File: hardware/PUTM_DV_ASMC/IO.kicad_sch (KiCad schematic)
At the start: 0 parts

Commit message: io section
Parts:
- added C29, C30: 100n, Capacitor_SMD:C_0603_1608Metric_Pad1.08x0.95mm_HandSolder, symbol Device:C_Small
- added Q?: BUK6D210, Local_Library:Diodes_UDFN2020-6_Type-F, symbol BUK6D210:BUK6D210
- added R3, R5: 2k, Resistor_SMD:R_0603_1608Metric_Pad0.98x0.95mm_HandSolder, symbol Device:R_Small
- added R4, R8: 10k, Resistor_SMD:R_0603_1608Metric_Pad0.98x0.95mm_HandSolder, symbol Device:R_Small
- added R?: 100R, Resistor_SMD:R_0603_1608Metric, symbol Device:R_Small
- added R?: 10k, Resistor_SMD:R_0603_1608Metric, symbol Device:R_Small
- added TP?: TestPoint_Small, TestPoint:TestPoint_Pad_D1.0mm, symbol Connector:TestPoint_Small
- added U3, U4: TLP291-4, Package_SO:SOIC-16_4.55x10.3mm_P1.27mm, symbol Isolator:TLP291-4
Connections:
- new net: Q?.3 (G), R?.1, R?.2, TP?.1
- new net: C30.1, R5.2, U4.1
- new net: C29.1, R3.2, U3.1
- new net +3.3V: R4.1, R8.1
- new net AS_SAFETY: R3.1
- new net AS_SENSE: R4.2, U3.16
- new net GND: C29.2, C30.2, Q?.4 (S), Q?.8 (S), R?.1, U3.15, U3.2, U4.15, U4.2
- new net IN_BUZZER: R?.2
- new net OUT_BUZZER: Q?.1 (D), Q?.2 (D), Q?.5 (D), Q?.6 (D), Q?.7 (D)
- new net RES_SAFETY: R5.1
- new net RES_SENSE: R8.2, U4.16
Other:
- note added: "+24V"
- note added: "Buzzer"
- note added: "Buzzer Section"
- note added: "Safety Sensig"
- title: (none) -> Input/Output Section

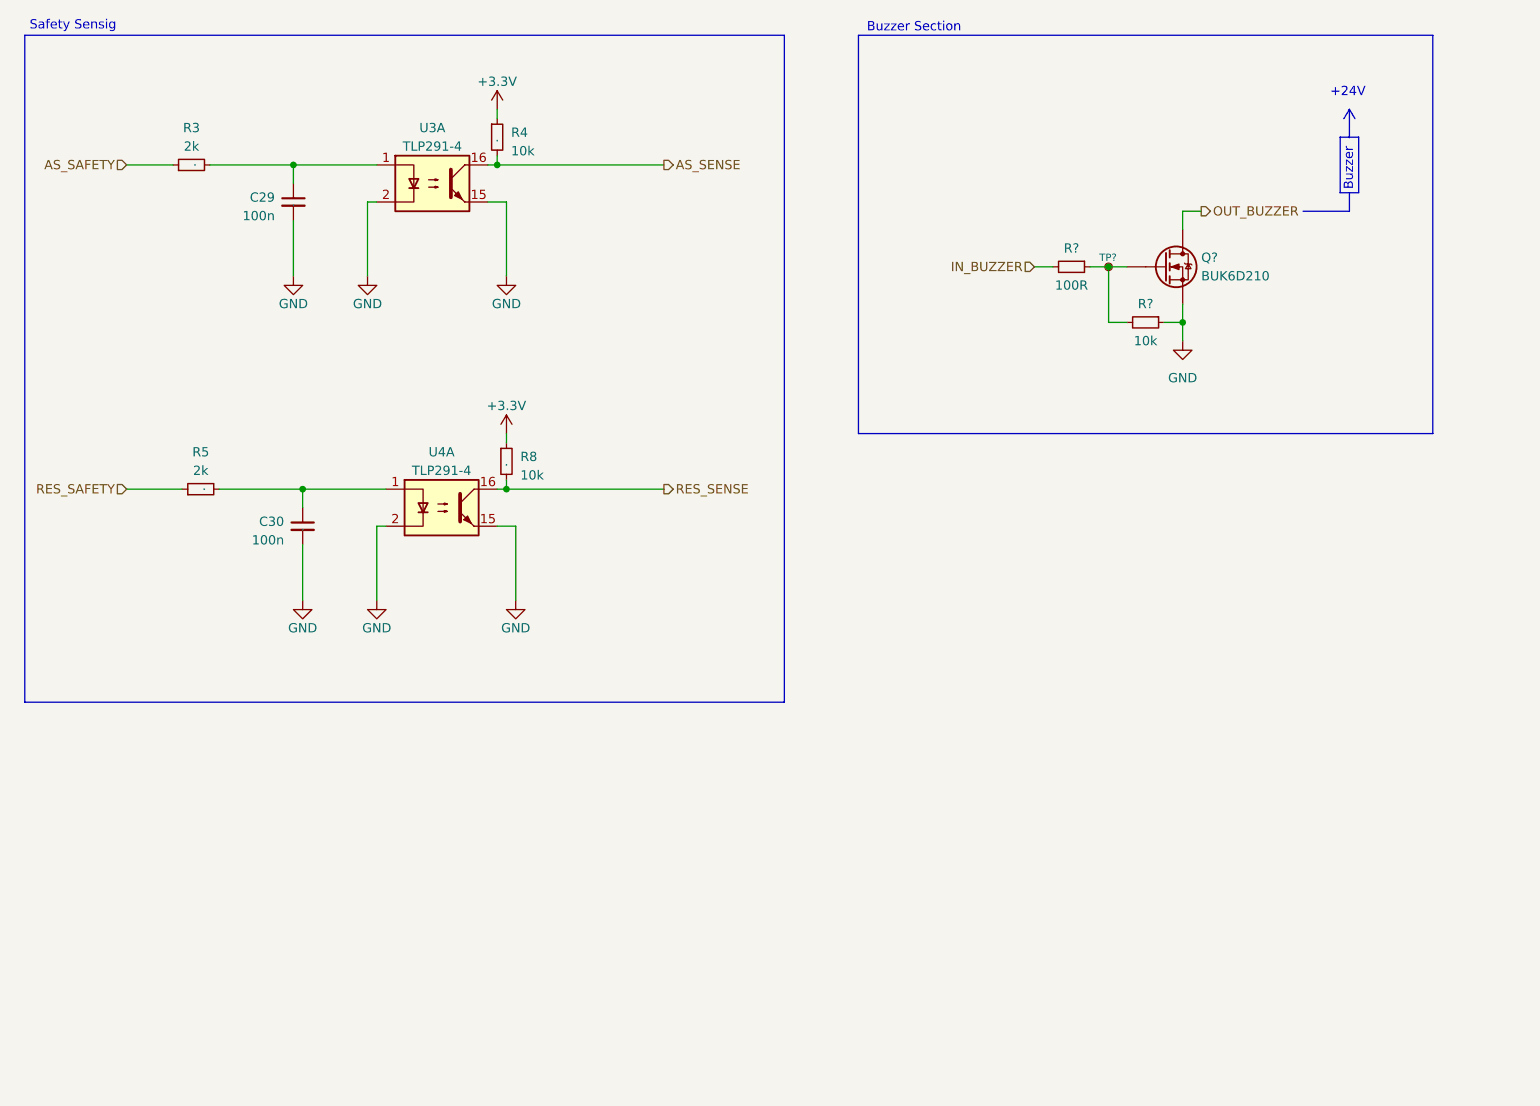
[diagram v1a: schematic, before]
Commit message: schematics without main connector
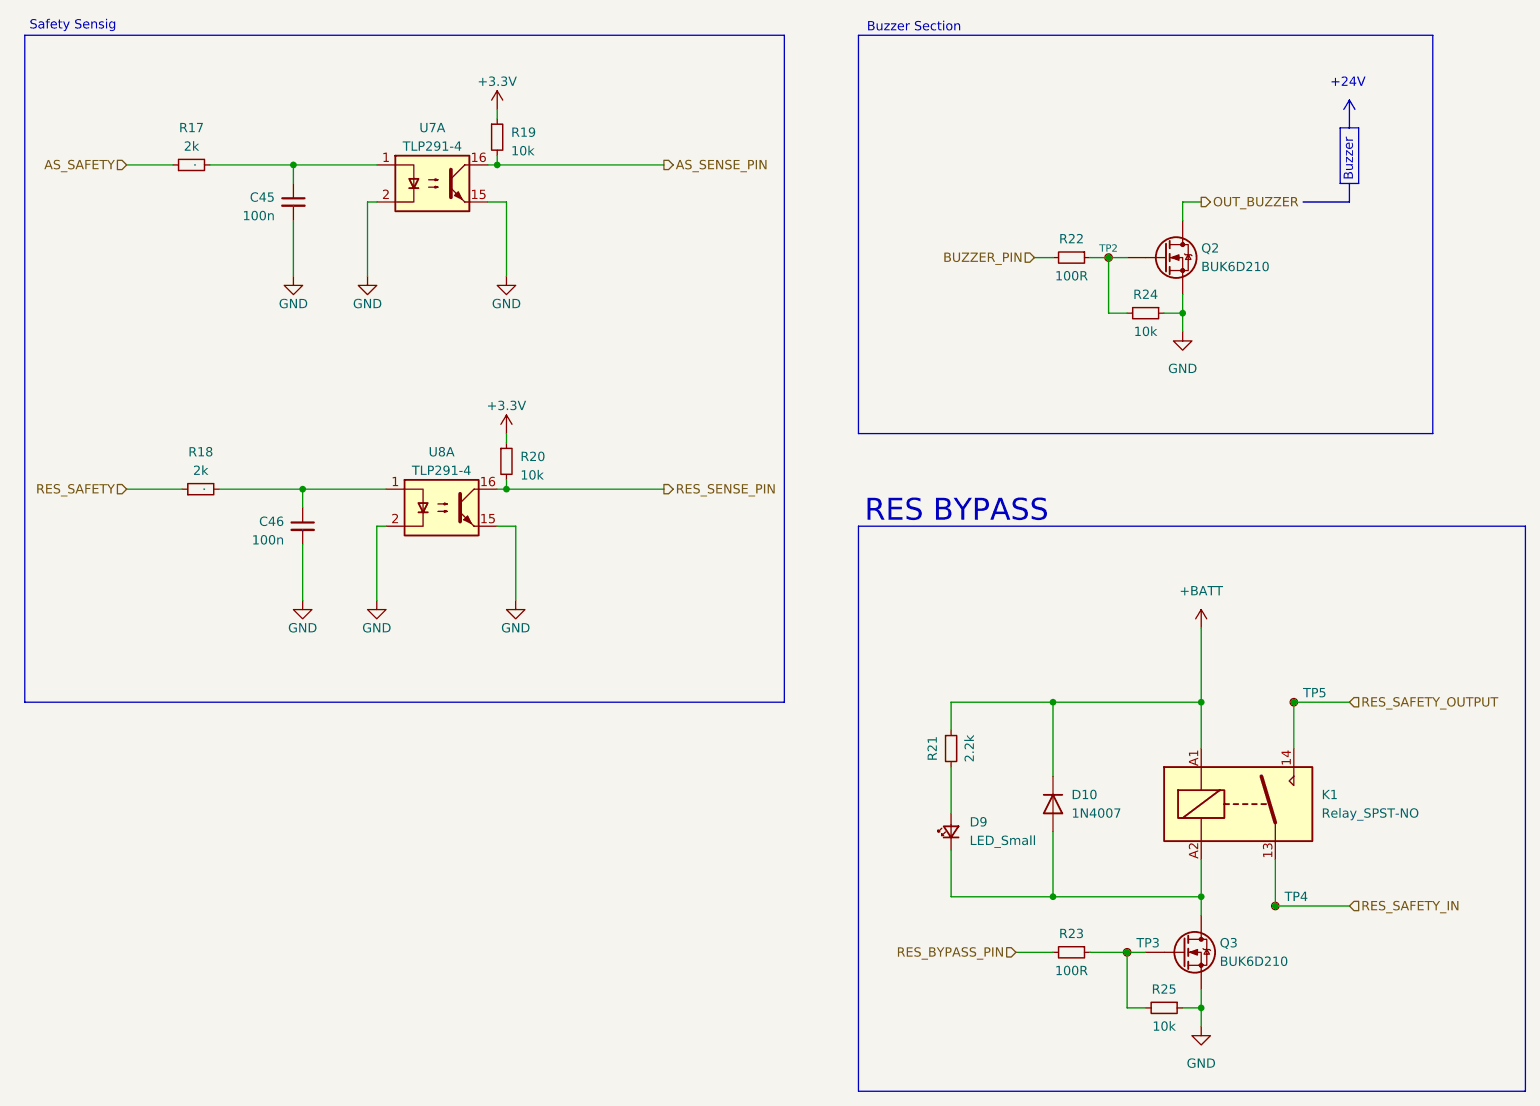
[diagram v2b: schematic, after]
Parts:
- added D10: 1N4007, Diode_THT:D_DO-41_SOD81_P10.16mm_Horizontal, symbol Diode:1N4007
- added D9: LED_Small, symbol Device:LED_Small
- added K1: Relay_SPST-NO, symbol Relay:Relay_SPST-NO
- added Q3: BUK6D210, Local_Library:Diodes_UDFN2020-6_Type-F, symbol BUK6D210:BUK6D210
- added R21: 2.2k, Resistor_SMD:R_1206_3216Metric_Pad1.30x1.75mm_HandSolder, symbol Device:R_Small
- added R23: 100R, Resistor_SMD:R_0603_1608Metric, symbol Device:R_Small
- added R25: 10k, Resistor_SMD:R_0603_1608Metric, symbol Device:R_Small
- added TP3, TP4, TP5: TestPoint_Small, symbol Connector:TestPoint_Small
- gave numbers to parts that had none: 4
- renumbered C29 to C45, C30 to C46, R3 to R17, R5 to R18, R4 to R19, R8 to R20, U3 to U7, U4 to U8
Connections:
- net GND: now also Q3.4 (S), Q3.8 (S), R25.1
- net AS_SENSE renamed AS_SENSE_PIN
- net IN_BUZZER renamed BUZZER_PIN
- net RES_SENSE renamed RES_SENSE_PIN
- new net: Q3.3 (G), R23.1, R25.2, TP3.1
- new net: D10.2 (A), D9.1 (K), K1.A2, Q3.1 (D), Q3.2 (D), Q3.5 (D), Q3.6 (D), Q3.7 (D)
- new net: D9.2 (A), R21.2
- new net +BATT: D10.1 (K), K1.A1, R21.1
- new net RES_BYPASS_PIN: R23.2
- new net RES_SAFETY_IN: K1.13, TP4.1
- new net RES_SAFETY_OUTPUT: K1.14, TP5.1
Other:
- note added: "RES BYPASS"
- moved on the sheet: Q2, R22, R24, TP2

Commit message: done schematic v1
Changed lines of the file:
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@@
 	)
 	(hierarchical_label "RES_SAFETY_OUTPUT"
-		(shape input)
+		(shape output)
 		(at 201.93 109.22 0)
 		(effects
@@
 	)
 	(hierarchical_label "RES_SAFETY_IN"
-		(shape input)
+		(shape output)
 		(at 201.93 137.16 0)
 		(effects
@@
 		)
 	)
-	(group ""
-		(members "058c119b-7b5e-4be6-9dd9-77956af8631e" "06eb6851-f71e-48c3-9d55-6a4454f72066"
-			"0f04764c-a9c6-4546-b0f8-8e79def7ef79" "1be2d804-d21b-42bf-9922-a1e309fc6313"
-			"20d4376f-85fc-438f-80fd-76ed747431a7" "2517ebd4-1633-4649-af89-dcdf95830b6f"
-			"2883a0e1-238c-42ef-9bbf-5d3af29825bc" "334e8cb6-5bb3-435d-9903-589fd98b6398"
-			"3df0cd19-b65c-417f-a0fd-361945718dc4" "3eab420e-4a45-4a70-855a-c900c3a10dd2"
-			"3fe88a36-0125-48db-a28f-10e085086908" "4a3b0eae-4bff-4e5b-a0b4-a98859ab8fae"
-			"4c7c4c9c-1cf3-4004-9802-0db4d4e54b92" "51e78d01-08dc-4f48-afe4-2cb2bb5cd559"
-			"58fcd43b-4f94-4f07-8bf2-a616202ffac8" "5c459c4a-ac80-46d9-b66f-ce0857e02798"
-			"6d31a3b8-99e6-4b49-8c53-aff4336e20b8" "6dbf84d3-72af-48e1-92f4-2f8d24832782"
-			"7048251e-2d57-4c7a-abd6-8eb55bf87aa3" "a109052a-2f62-481d-8364-96d638b9e39b"
-			"a16fcd44-259b-4214-93f9-ce0456dfff68" "a55c4ed3-f659-4865-82be-744633d19361"
-			"ab5d48bf-d740-4920-b823-31d1c89de7ce" "ab722c10-840f-46a0-89b6-ca8210a4b5f0"
-			"b00dd03d-f6f1-4cee-8322-05d2814af237" "bd5c868e-759a-451f-a8fa-e3902719da1d"
-			"d454ba87-598c-4b5e-ae94-e0a08750598a" "e149af7e-e9bc-482f-837a-7105fe1d689c"
-			"e560e48f-4926-43a8-aca3-5d48b251c2f7" "e86e67bc-af59-4abf-91fb-ea473bbc48ce"
-			"f8eda6d1-aa82-4881-a45a-fa8cb19e135d"
-		)
-	)

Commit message: schematic without error
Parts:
- removed U7: TLP291-4, Package_SO:SOIC-16_4.55x10.3mm_P1.27mm, symbol Isolator:TLP291-4
- added unit 2 of U8
- Q2, Q3: footprint Local_Library:Diodes_UDFN2020-6_Type-F -> UDFN2020-6:Diodes_UDFN2020-6_Type-F
- U8: Mouser Part Number 757-TLP293-4TPRE -> (none)
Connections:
- net AS_SENSE_PIN: now also U8.16
- net GND: now also U8.13, U8.4
- net RES_SENSE_PIN: now also U8.14; no longer U8.16
- net at C46.1, R18.2: now also U8.3; no longer U8.1
- net at C45.1, R17.2: now also U8.1

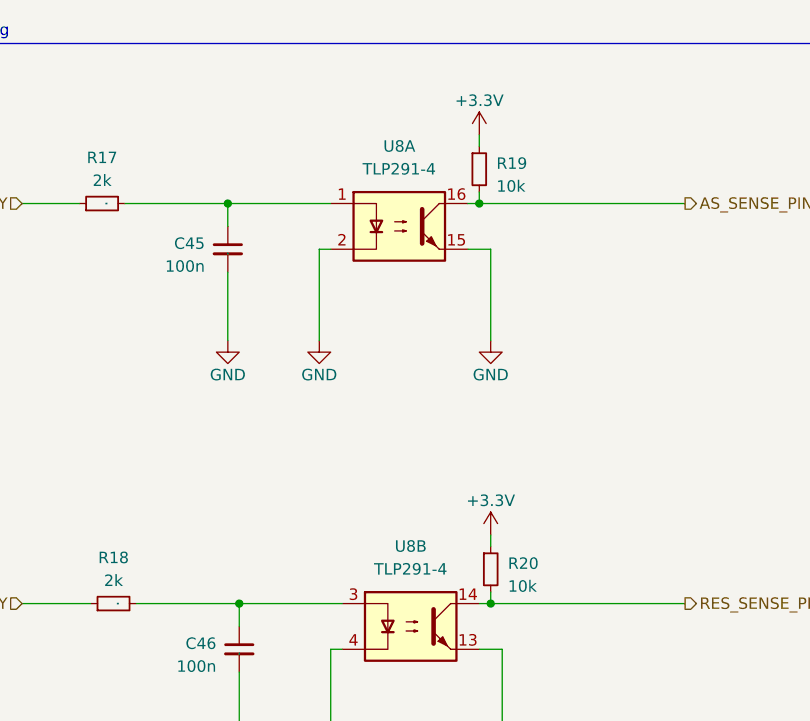
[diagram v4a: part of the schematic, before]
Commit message: tylko dwa bledy z can - schemat na wykonczeniu
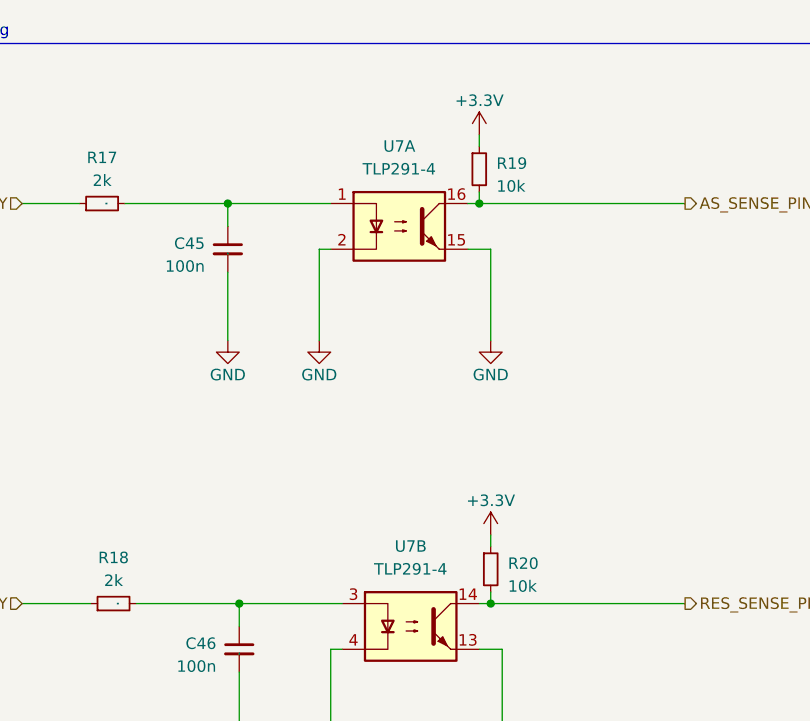
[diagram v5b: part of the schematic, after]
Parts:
- renumbered U8 to U7
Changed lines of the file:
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@@
 		(dnp no)
 		(fields_autoplaced yes)
-		(property "Reference" "U8"
+		(property "Reference" "U7"
 			(at 77.47 73.66 0)
 			(show_name no)
@@
 			(project "PUTM_DV_ASMC"
 				(path "/b652b05a-4e3d-4ad1-b032-18886abe7d45/758e311c-7b96-4a6d-a057-b3755526b6e1"
-					(reference "U8")
+					(reference "U7")
 					(unit 2)
 				)
@@
 		(dnp no)
 		(fields_autoplaced yes)
-		(property "Reference" "U8"
+		(property "Reference" "U7"
 			(at 76.2 29.21 0)
 			(show_name no)
@@
 			(project "PUTM_DV_ASMC"
 				(path "/b652b05a-4e3d-4ad1-b032-18886abe7d45/758e311c-7b96-4a6d-a057-b3755526b6e1"
-					(reference "U8")
-					(unit 1)
-				)
+					(reference "U7")
+					(unit 1)
+				)

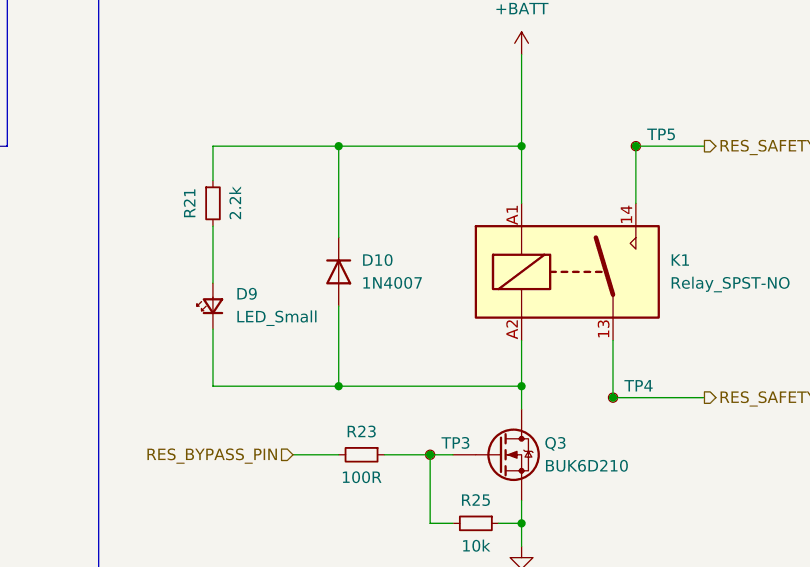
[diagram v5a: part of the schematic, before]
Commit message: poprawki footprint
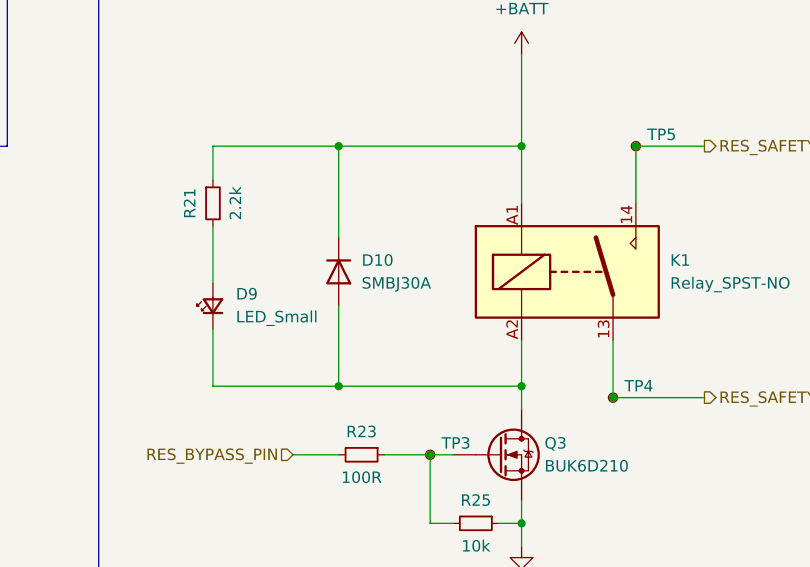
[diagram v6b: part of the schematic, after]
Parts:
- D10: value 1N4007 -> SMBJ30A; footprint Diode_THT:D_DO-41_SOD81_P10.16mm_Horizontal -> Diode_SMD:D_SMB_Handsoldering
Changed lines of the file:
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@@
 			)
 		)
-		(property "Value" "1N4007"
+		(property "Value" "SMBJ30A"
 			(at 163.83 124.4599 90)
 			(show_name no)
@@
 			)
 		)
-		(property "Footprint" "Diode_THT:D_DO-41_SOD81_P10.16mm_Horizontal"
+		(property "Footprint" "Diode_SMD:D_SMB_Handsoldering"
 			(at 156.845 123.19 0)
 			(hide yes)
@@
 			)
 		)
-		(property "Datasheet" "http://www.vishay.com/docs/88503/1n4001.pdf"
+		(property "Datasheet" "https://www.vishay.com/docs/88392/smbj.pdf"
 			(at 161.29 123.19 0)
 			(hide yes)
@@
 			)
 		)
-		(property "Description" "1000V 1A General Purpose Rectifier Diode, DO-41"
+		(property "Description" "ESD Protection Diodes / TVS Diodes 30V 1000W UniDir TransZorb 5% Tol"
 			(at 161.29 123.19 0)
 			(hide yes)

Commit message: make zones
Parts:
- removed D10: SMBJ30A, Diode_SMD:D_SMB_Handsoldering, symbol Diode:1N4007
- removed D9: LED_Small, symbol Device:LED_Small
- removed K1: Relay_SPST-NO, symbol Relay:Relay_SPST-NO
- removed U7: TLP291-4, Package_SO:SOIC-16_4.55x10.3mm_P1.27mm, symbol Isolator:TLP291-4
- added D10: D_Small, Diode_SMD:D_0805_2012Metric_Pad1.15x1.40mm_HandSolder, symbol Device:D_Small
- added D9: LED, LED_SMD:LED_0603_1608Metric_Pad1.05x0.95mm_HandSolder, symbol Device:LED
- added K2: FINDER-32.21-x000, Relay_THT:Relay_SPDT_Finder_32.21-x000, symbol Relay:FINDER-32.21-x000
- added U14, U15: FODM217B, Package_SO:SOP-4_4.4x2.6mm_P1.27mm, symbol Isolator:FODM217B
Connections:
- net +BATT: now also D10.1 (K), K2.A1; no longer R21.1
- net AS_SENSE_PIN: now also U14.4
- net GND: now also D9.1 (K), U14.2, U14.3, U15.2, U15.3
- net RES_SAFETY_IN: now also K2.11
- net RES_SAFETY_OUTPUT: now also R21.1, K2.14
- net RES_SENSE_PIN: now also U15.4
- net at C46.1, R18.2: now also U15.1
- net at Q3.1 (D), Q3.2 (D), Q3.5 (D)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: now also D10.2 (A), K2.A2
- net at R21.2: now also D9.2 (A)
- net at C45.1, R17.2: now also U14.1
- no-connect marks 0 -> 1
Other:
- moved on the sheet: TP4, TP5
